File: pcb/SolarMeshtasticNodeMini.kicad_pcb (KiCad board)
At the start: 4 copper layers, 33 x 47 mm, 31 parts, among them J2 Conn_01x02_Socket, J3 Conn_01x04_Socket, J4 Conn_01x02_Pin, J5 Conn_01x04_Socket, SW1 SSSS811101, SW2 SW_Push, U1 BQ25185, U2 HT-CT62, U3 HE9073A30MR, U4 APX803L05-32SA-7, U9 SS26_C5350986

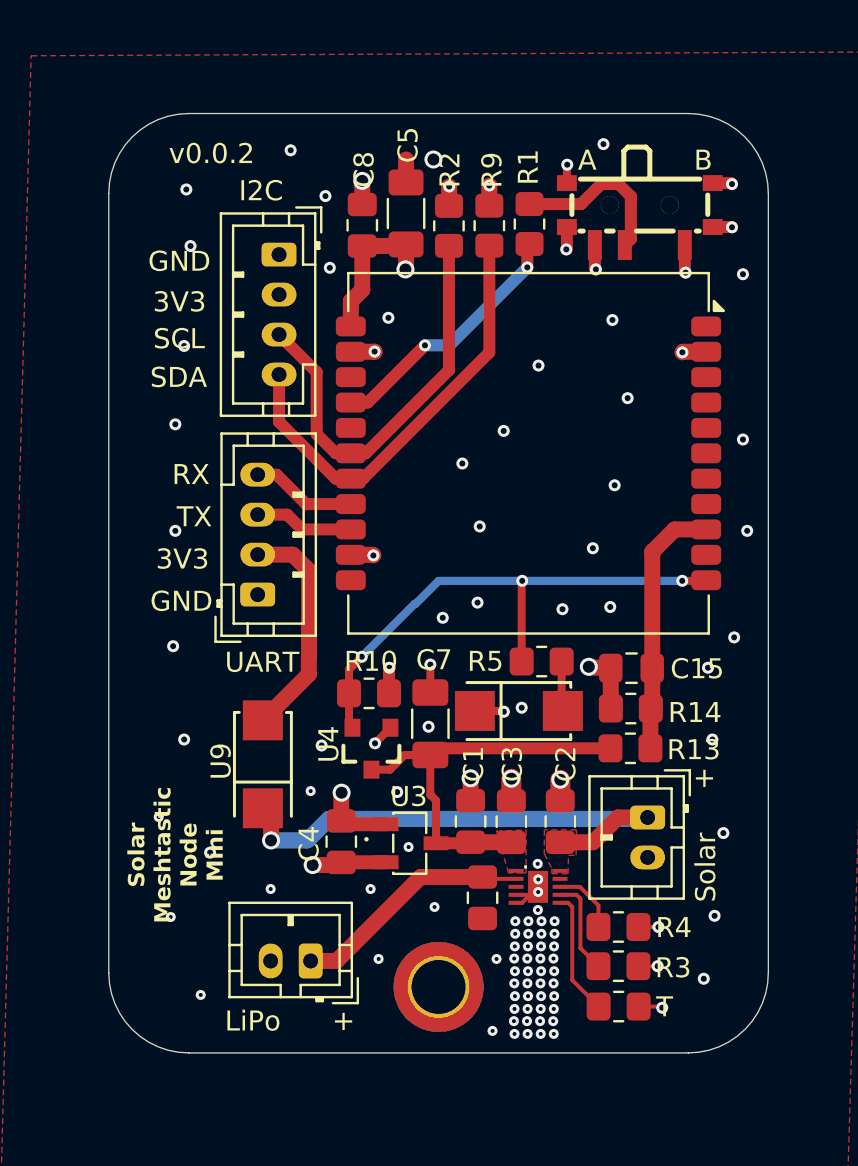
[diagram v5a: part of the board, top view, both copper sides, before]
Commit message: pcb, sch: other hole size and re-center
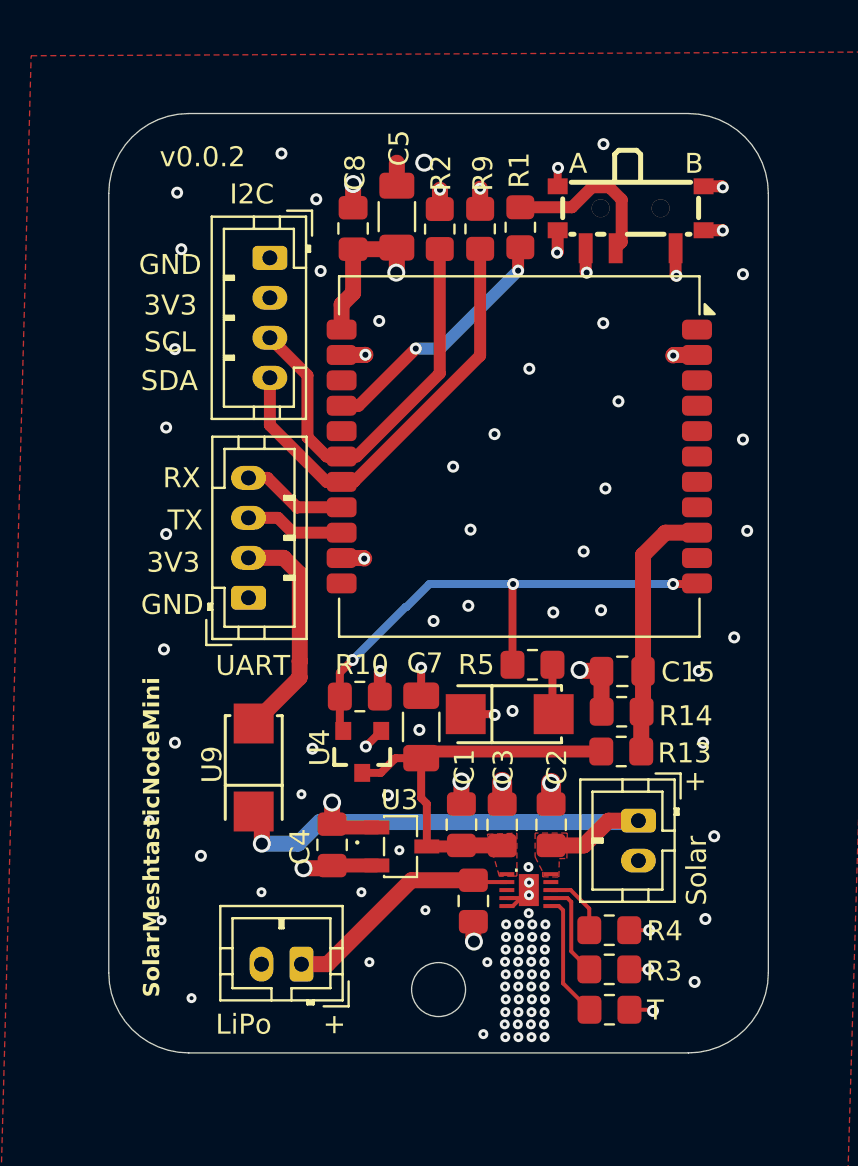
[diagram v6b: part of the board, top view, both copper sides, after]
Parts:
- H1: footprint MountingHole:MountingHole_2.7mm_M2.5_ISO14580_Pad_TopBottom -> MountingHole:MountingHole_2.7mm_M2.5_ISO7380
- moved R10 0.49 mm to (224.1, 59.2)
- moved R13 0.49 mm to (237.1, 61.9)
- moved R2 0.49 mm to (228.1, 35.8)
- moved C15 0.49 mm to (237.2, 57.9)
- moved C2 0.49 mm to (233.6, 65.6)
- moved C3 0.49 mm to (231.2, 65.6)
- moved C7 0.49 mm to (227.1, 60.7)
- moved J2 0.49 mm to (238.0, 65.4)
- moved J4 0.49 mm to (221.1, 72.6)
- moved J5 0.49 mm to (219.6, 37.2)
- moved R1 0.49 mm to (232.1, 35.7)
- moved R14 0.49 mm to (237.2, 59.9)
- moved R3 0.49 mm to (236.5, 72.8)
- moved R4 0.49 mm to (236.5, 70.9)
- moved R5 0.49 mm to (232.7, 57.6)
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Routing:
- net GND: track 30.4 -> 31.1 mm, vias 114 -> 115
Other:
- board text added: "SolarMeshtasticNodeMini"
- board text removed: "Solar Meshtastic Node Mini"

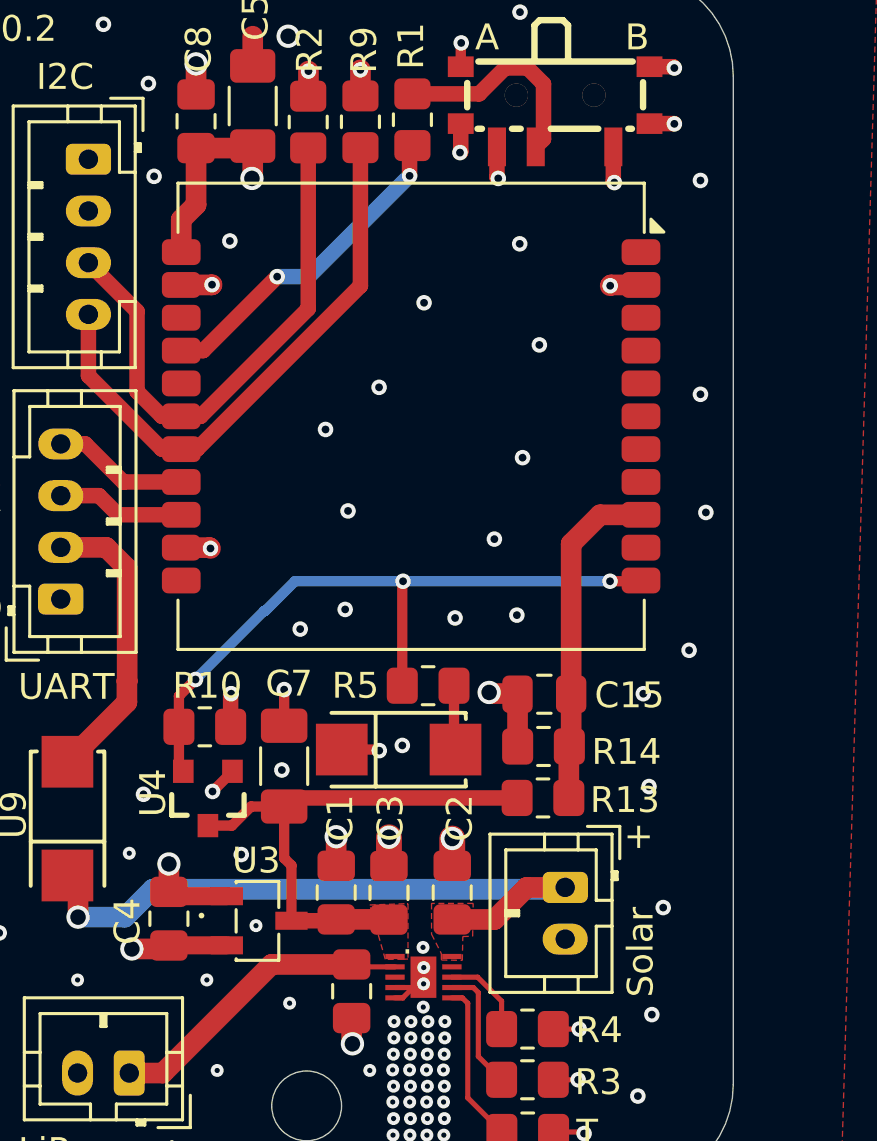
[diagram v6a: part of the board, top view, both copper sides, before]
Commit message: pcb: mark 2.4GHz u.fl connector with a silk print
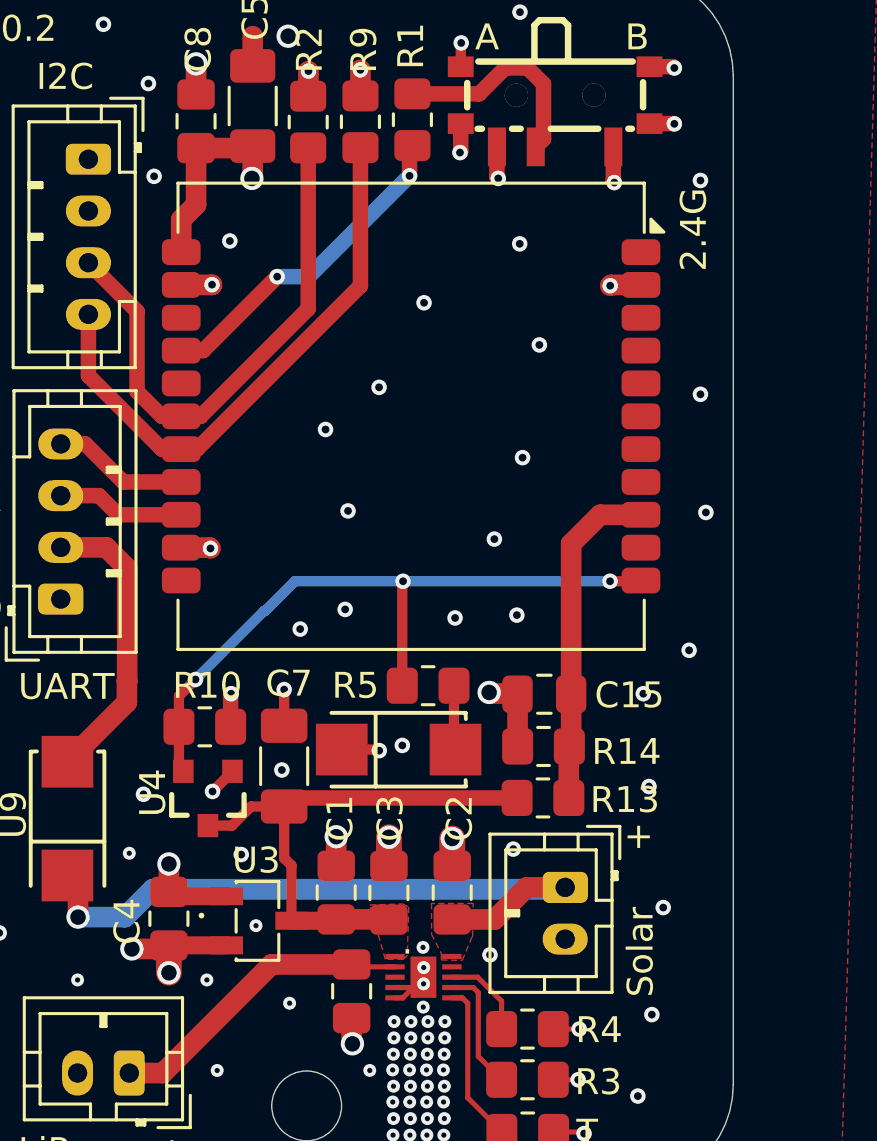
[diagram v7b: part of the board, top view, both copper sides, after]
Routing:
- net +3V3: track 15.4 -> 16.3 mm, vias 6 -> 7
- net GND: vias 115 -> 117
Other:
- board text added: "2.4G"
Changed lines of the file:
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@@
+		)
+	)
+	(gr_text "2.4G"
+		(at 243.56 41.56 90)
+		(layer "F.SilkS")
+		(effects
+			(font
+				(size 1 1)
+				(thickness 0.125)
+			)
+			(justify left bottom)
 		)
 	)
@@
 		(start 227.4125 66.67)
 		(end 229.09 66.67)
-		(width 0.6)
+		(width 0.7)
 		(layer "F.Cu")
 		(net 1)
@@
 	)
 	(via
+		(at 235.09 67.99)
+		(size 0.6)
+		(drill 0.3)
+		(layers "F.Cu" "B.Cu")
+		(free yes)
+		(net 2)
+	)
+	(via
 		(at 232.67 73.07)
 		(size 0.5)
@@
 	)
 	(via
+		(at 235.99 63.9)
+		(size 0.6)
+		(drill 0.3)
+		(layers "F.Cu" "B.Cu")
+		(free yes)
+		(net 2)
+	)
+	(via
 		(at 232.01 71.83)
 		(size 0.5)
@@
 	)
 	(segment
-		(start 229.8325 68.4525)
-		(end 229.74 68.36)
-		(width 0.2)
-		(layer "F.Cu")
-		(net 3)
-	)
-	(segment
 		(start 226.64 68.36)
 		(end 222.44 72.56)
@@
 	)
 	(segment
-		(start 237.93 65.45)
-		(end 238 65.38)
-		(width 0.8)
-		(layer "B.Cu")
-		(net 22)
-	)
-	(segment
 		(start 234.639 69.4461)
 		(end 234.4454 69.2525)
@@
 	)
 	(segment
-		(start 222.54 67.76)
-		(end 222.6725 67.6275)
-		(width 0.8)
-		(layer "F.Cu")
-		(net 28)
-	)
-	(segment
 		(start 235.36 36.74)
 		(end 235.36 37.91)
@@
 	)
 	(segment
+		(start 222.6725 67.6275)
+		(end 222.6725 68.6825)
+		(width 1)
+		(layer "F.Cu")
+		(net 28)
+	)
+	(segment
 		(start 223.15 39.552934)
 		(end 223.15 40.81)
@@
 		(width 0.8)
 		(layer "F.Cu")
+		(net 28)
+	)
+	(via
+		(at 222.6725 68.6825)
+		(size 0.9)
+		(drill 0.6)
+		(layers "F.Cu" "B.Cu")
 		(net 28)
 	)
@@
 	)
 	(segment
-		(start 238.23 59.86)
-		(end 238.16 59.93)
-		(width 0.8)
-		(layer "F.Cu")
-		(net 30)
-	)
-	(segment
 		(start 238.23 57.91)
 		(end 238.23 52.09)
@@
 		(start 238.23 57.91)
 		(end 238.23 59.86)
-		(width 0.8)
-		(layer "F.Cu")
-		(net 30)
-	)
-	(segment
-		(start 238.14 59.95)
-		(end 238.16 59.93)
 		(width 0.8)
 		(layer "F.Cu")
@@
 		(polygon
 			(pts
-				(xy 231.74 68.16) (xy 231.04 68.16) (xy 230.44 66.06) (xy 231.88 66.01) (xy 231.92 66.01) (xy 231.92 68.15)
+				(xy 231.74 68.16) (xy 231.04 68.16) (xy 230.44 66.06) (xy 231.72 66.02) (xy 231.95 66.14) (xy 231.89 68.02)
 			)
 		)
@@
 		(polygon
 			(pts
-				(xy 232.83 66) (xy 232.83 67.19) (xy 233.21 67.94) (xy 233.21 68.19) (xy 234.02 68.2) (xy 234.04 67.28)
+				(xy 232.83 66) (xy 232.83 67.19) (xy 233.21 67.94) (xy 233.21 68.19) (xy 234.02 68.2) (xy 234.38 67.33)
 				(xy 234.42 67.27) (xy 234.44 66)
 			)

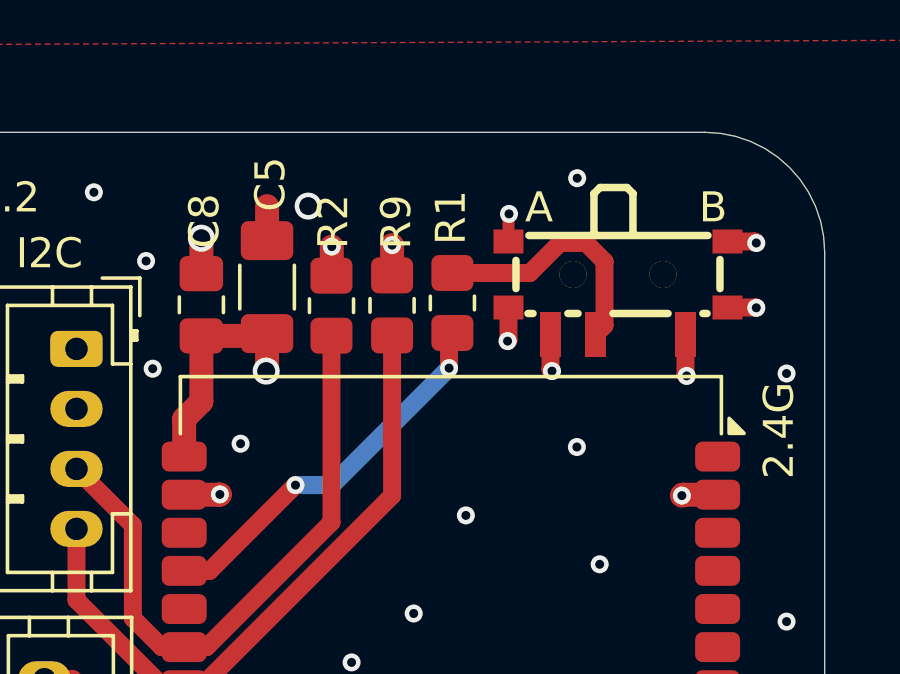
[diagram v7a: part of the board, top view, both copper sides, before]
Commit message: pcb,sch: make the 3v3 of the bootloader switch weaker
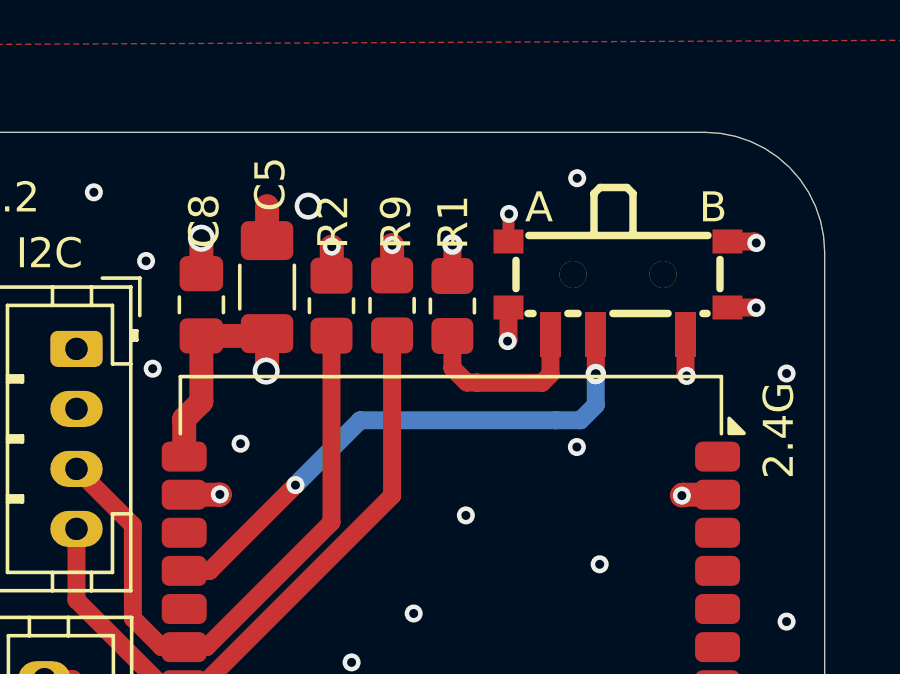
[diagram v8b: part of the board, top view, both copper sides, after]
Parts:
- R1: value R -> 10k
- moved R1 0.10 mm to (232.1, 35.8), turned to 90 degrees
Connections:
- R1 pad 2: /ESP32_BOOTLOADER_MODE_1 -> +3V3
- SW1 pad 2: Net-(R1-Pad1) -> /ESP32_BOOTLOADER_MODE_1
- SW1 pad 3: +3V3 -> Net-(R1-Pad1)
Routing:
- net /ESP32_BOOTLOADER_MODE_1: track 12.7 -> 18.4 mm
- net Net-(R1-Pad1): track 8.30 -> 5.99 mm
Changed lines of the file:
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@@
 	(footprint "Resistor_SMD:R_0805_2012Metric_Pad1.20x1.40mm_HandSolder"
 		(layer "F.Cu")
-		(at 232.09 35.69 -90)
+		(at 232.09 35.79 90)
 		(descr "Resistor SMD 0805 (2012 Metric), square (rectangular) end terminal, IPC-7351 nominal with elongated pad for handsoldering. (Body size source: IPC-SM-782 page 72, https://www.pcb-3d.com/wordpress/wp-content/uploads/ipc-sm-782a_amendment_1_and_2.pdf), generated with kicad-footprint-generator")
 		(tags "resistor handsolder")
 		(property "Reference" "R1"
-			(at -2.85 0.05 90)
+			(at 2.79 0.03 90)
 			(layer "F.SilkS")
 			(effects
@@
 			)
 		)
-		(property "Value" "R"
+		(property "Value" "10k"
 			(at 0 1.65 90)
 			(layer "F.Fab")
@@
 		(attr smd)
 		(fp_line
-			(start -0.227064 0.735)
-			(end 0.227064 0.735)
+			(start -0.227064 -0.735)
+			(end 0.227064 -0.735)
 			(stroke
 				(width 0.12)
@@
 		)
 		(fp_line
-			(start -0.227064 -0.735)
-			(end 0.227064 -0.735)
+			(start -0.227064 0.735)
+			(end 0.227064 0.735)
 			(stroke
 				(width 0.12)
@@
 		)
 		(fp_line
-			(start -1.85 0.95)
-			(end -1.85 -0.95)
+			(start 1.85 -0.95)
+			(end 1.85 0.95)
 			(stroke
 				(width 0.05)
@@
 		)
 		(fp_line
-			(start 1.85 0.95)
-			(end -1.85 0.95)
+			(start -1.85 -0.95)
+			(end 1.85 -0.95)
 			(stroke
 				(width 0.05)
@@
 		)
 		(fp_line
-			(start -1.85 -0.95)
-			(end 1.85 -0.95)
+			(start 1.85 0.95)
+			(end -1.85 0.95)
 			(stroke
 				(width 0.05)
@@
 		)
 		(fp_line
-			(start 1.85 -0.95)
-			(end 1.85 0.95)
+			(start -1.85 0.95)
+			(end -1.85 -0.95)
 			(stroke
 				(width 0.05)
@@
 		)
 		(fp_line
-			(start -1 0.625)
-			(end -1 -0.625)
+			(start 1 -0.625)
+			(end 1 0.625)
 			(stroke
 				(width 0.1)
@@
 		)
 		(fp_line
-			(start 1 0.625)
-			(end -1 0.625)
+			(start -1 -0.625)
+			(end 1 -0.625)
 			(stroke
 				(width 0.1)
@@
 		)
 		(fp_line
-			(start -1 -0.625)
-			(end 1 -0.625)
+			(start 1 0.625)
+			(end -1 0.625)
 			(stroke
 				(width 0.1)
@@
 		)
 		(fp_line
-			(start 1 -0.625)
-			(end 1 0.625)
+			(start -1 0.625)
+			(end -1 -0.625)
 			(stroke
 				(width 0.1)
@@
 		)
 		(pad "1" smd roundrect
-			(at -1 0 270)
+			(at -1 0 90)
 			(size 1.2 1.4)
 			(layers "F.Cu" "F.Mask" "F.Paste")
@@
 		)
 		(pad "2" smd roundrect
-			(at 1 0 270)
+			(at 1 0 90)
 			(size 1.2 1.4)
 			(layers "F.Cu" "F.Mask" "F.Paste")
 			(roundrect_rratio 0.208333)
-			(net 4 "/ESP32_BOOTLOADER_MODE_1")
+			(net 28 "+3V3")
 			(pintype "passive")
 		)
@@
 			(size 0.7 1.5)
 			(layers "F.Cu" "F.Mask" "F.Paste")
-			(net 8 "Net-(R1-Pad1)")
+			(net 4 "/ESP32_BOOTLOADER_MODE_1")
 			(pinfunction "2")
 			(pintype "unspecified")
@@
 			(size 0.7 1.5)
 			(layers "F.Cu" "F.Mask" "F.Paste")
-			(net 28 "+3V3")
+			(net 8 "Net-(R1-Pad1)")
 			(pinfunction "3")
 			(pintype "unspecified")
@@
 	)
 	(segment
-		(start 231.98 37.86)
-		(end 231.98 36.8)
+		(start 224 44.62)
+		(end 226.86 41.76)
 		(width 0.6)
 		(layer "F.Cu")
@@
 	)
 	(segment
-		(start 224 44.62)
-		(end 226.86 41.76)
+		(start 223.15 44.62)
+		(end 224 44.62)
 		(width 0.6)
 		(layer "F.Cu")
@@
 	)
 	(segment
-		(start 223.15 44.62)
-		(end 224 44.62)
+		(start 236.87 38.06)
+		(end 236.87 36.75)
+		(width 0.6)
+		(layer "F.Cu")
+		(net 4)
+	)
+	(segment
+		(start 236.87 36.75)
+		(end 236.86 36.74)
 		(width 0.6)
 		(layer "F.Cu")
@@
 	)
 	(via
-		(at 226.86 41.76)
-		(size 0.6)
-		(drill 0.3)
+		(at 236.87 38.06)
+		(size 0.6858)
+		(drill 0.3302)
 		(layers "F.Cu" "B.Cu")
 		(net 4)
 	)
 	(via
-		(at 231.98 37.86)
+		(at 226.86 41.76)
 		(size 0.6)
 		(drill 0.3)
@@
 	(segment
 		(start 226.86 41.76)
-		(end 228.08 41.76)
+		(end 229.02 39.6)
 		(width 0.6)
 		(layer "B.Cu")
@@
 	)
 	(segment
-		(start 228.08 41.76)
-		(end 231.98 37.86)
+		(start 236.87 39.09)
+		(end 236.87 38.06)
+		(width 0.6)
+		(layer "B.Cu")
+		(net 4)
+	)
+	(segment
+		(start 229.02 39.6)
+		(end 235.53 39.6)
+		(width 0.6)
+		(layer "B.Cu")
+		(net 4)
+	)
+	(segment
+		(start 235.53 39.6)
+		(end 236.36 39.6)
+		(width 0.6)
+		(layer "B.Cu")
+		(net 4)
+	)
+	(segment
+		(start 236.36 39.6)
+		(end 236.87 39.09)
 		(width 0.6)
 		(layer "B.Cu")
@@
 	)
 	(segment
-		(start 237.161 36.439)
-		(end 236.86 36.74)
+		(start 235.36 38.07)
+		(end 235.08 38.35)
 		(width 0.6)
 		(layer "F.Cu")
@@
 	)
 	(segment
-		(start 237.161 34.304662)
-		(end 237.161 36.439)
+		(start 235.08 38.35)
+		(end 232.92 38.35)
 		(width 0.6)
 		(layer "F.Cu")
@@
 	)
 	(segment
-		(start 232.09 34.69)
-		(end 234.673662 34.69)
+		(start 232.91 38.34)
+		(end 232.57 38.34)
 		(width 0.6)
 		(layer "F.Cu")
@@
 	)
 	(segment
-		(start 236.545338 33.689)
-		(end 237.161 34.304662)
+		(start 232.57 38.34)
+		(end 232.09 37.86)
 		(width 0.6)
 		(layer "F.Cu")
@@
 	)
 	(segment
-		(start 234.673662 34.69)
-		(end 235.674662 33.689)
+		(start 235.36 36.74)
+		(end 235.36 38.07)
 		(width 0.6)
 		(layer "F.Cu")
@@
 	)
 	(segment
-		(start 235.674662 33.689)
-		(end 236.545338 33.689)
+		(start 232.92 38.35)
+		(end 232.91 38.34)
+		(width 0.6)
+		(layer "F.Cu")
+		(net 8)
+	)
+	(segment
+		(start 232.09 37.86)
+		(end 232.09 36.79)
 		(width 0.6)
 		(layer "F.Cu")
@@
 	)
 	(segment
-		(start 235.36 36.74)
-		(end 235.36 37.91)
-		(width 0.6)
-		(layer "F.Cu")
-		(net 28)
-	)
-	(segment
 		(start 223.722934 36.7875)
 		(end 223.722934 38.98)
@@
 	)
 	(segment
-		(start 235.36 37.91)
-		(end 235.41 37.96)
+		(start 232.09 34.79)
+		(end 232.09 33.74)
 		(width 0.6)
 		(layer "F.Cu")
@@
 	)
 	(via
+		(at 232.09 33.74)
+		(size 0.6858)
+		(drill 0.3302)
+		(layers "F.Cu" "B.Cu")
+		(net 28)
+	)
+	(via
 		(at 221.24 67.76)
 		(size 0.9)
@@
 		(layers "F.Cu" "B.Cu")
 		(net 28)
-	)
-	(via
-		(at 235.41 37.96)
-		(size 0.6)
-		(drill 0.3)
-		(layers "F.Cu" "B.Cu")
-		(net 28)
